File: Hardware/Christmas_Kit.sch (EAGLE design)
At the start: 17 parts, among them U2 ATTINY13DIP, U4 AVR_SPI_PRG_6PTH

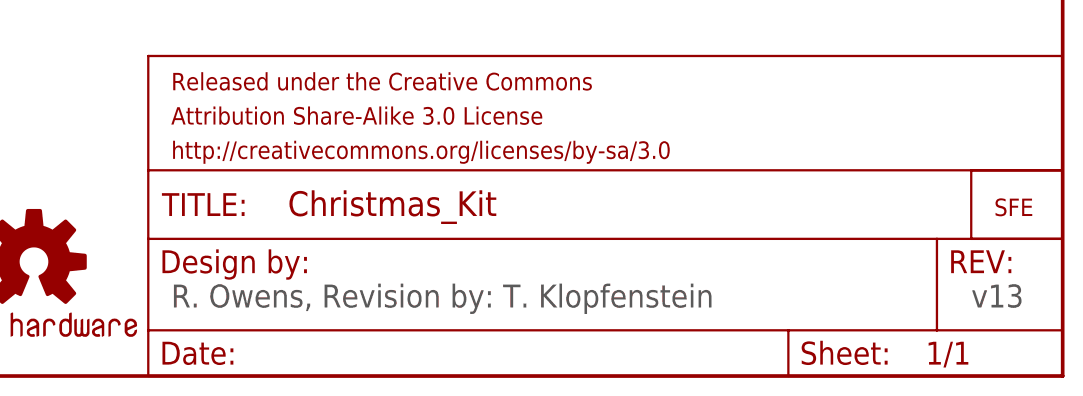
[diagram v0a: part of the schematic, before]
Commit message: Updated revision to symbol
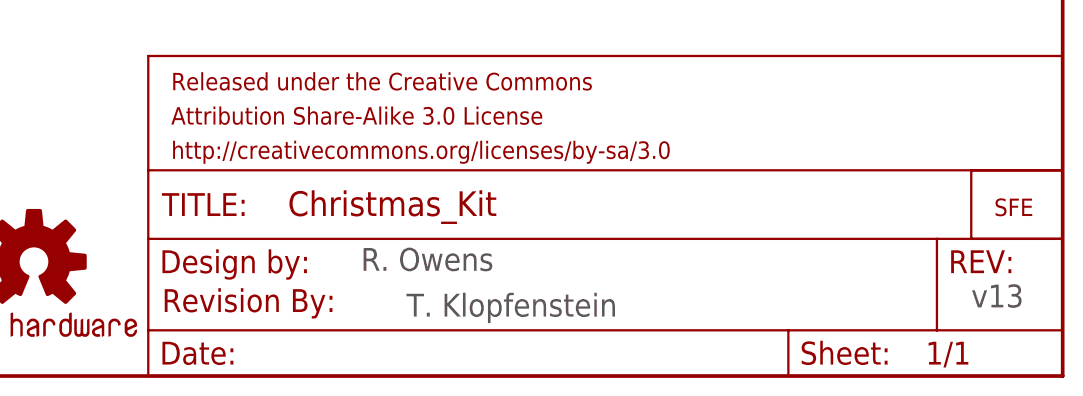
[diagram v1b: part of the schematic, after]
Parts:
- added U$1: REVISION, SparkFun-Aesthetics:REVISION
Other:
- note added: "R. Owens"
- note added: "T. Klopfenstein"
- note removed: "R. Owens, Revision by: T. Klopfenstein"
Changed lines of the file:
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@@
 <grid distance="0.1" unitdist="inch" unit="inch" style="lines" multiple="1" display="no" altdistance="0.01" altunitdist="inch" altunit="inch"/>
 <layers>
-<layer number="1" name="Top" color="4" fill="1" visible="yes" active="no"/>
-<layer number="2" name="Route2" color="1" fill="3" visible="yes" active="no"/>
-<layer number="3" name="Route3" color="4" fill="3" visible="yes" active="no"/>
-<layer number="4" name="Route4" color="1" fill="4" visible="yes" active="no"/>
-<layer number="5" name="Route5" color="4" fill="4" visible="yes" active="no"/>
-<layer number="6" name="Route6" color="1" fill="8" visible="yes" active="no"/>
-<layer number="7" name="Route7" color="4" fill="8" visible="yes" active="no"/>
-<layer number="8" name="Route8" color="1" fill="2" visible="yes" active="no"/>
-<layer number="9" name="Route9" color="4" fill="2" visible="yes" active="no"/>
-<layer number="10" name="Route10" color="1" fill="7" visible="yes" active="no"/>
-<layer number="11" name="Route11" color="4" fill="7" visible="yes" active="no"/>
-<layer number="12" name="Route12" color="1" fill="5" visible="yes" active="no"/>
-<layer number="13" name="Route13" color="4" fill="5" visible="yes" active="no"/>
-<layer number="14" name="Route14" color="1" fill="6" visible="yes" active="no"/>
-<layer number="15" name="Route15" color="4" fill="6" visible="yes" active="no"/>
-<layer number="16" name="Bottom" color="1" fill="1" visible="yes" active="no"/>
-<layer number="17" name="Pads" color="2" fill="1" visible="yes" active="no"/>
-<layer number="18" name="Vias" color="2" fill="1" visible="yes" active="no"/>
-<layer number="19" name="Unrouted" color="6" fill="1" visible="yes" active="no"/>
-<layer number="20" name="Dimension" color="15" fill="1" visible="yes" active="no"/>
-<layer number="21" name="tPlace" color="16" fill="1" visible="yes" active="no"/>
-<layer number="22" name="bPlace" color="14" fill="1" visible="yes" active="no"/>
-<layer number="23" name="tOrigins" color="15" fill="1" visible="yes" active="no"/>
-<layer number="24" name="bOrigins" color="15" fill="1" visible="yes" active="no"/>
-<layer number="25" name="tNames" color="7" fill="1" visible="yes" active="no"/>
-<layer number="26" name="bNames" color="7" fill="1" visible="yes" active="no"/>
-<layer number="27" name="tValues" color="7" fill="1" visible="yes" active="no"/>
-<layer number="28" name="bValues" color="7" fill="1" visible="yes" active="no"/>
+<layer number="1" name="Top" color="4" fill="1" visible="no" active="no"/>
+<layer number="2" name="Route2" color="1" fill="3" visible="no" active="no"/>
+<layer number="3" name="Route3" color="4" fill="3" visible="no" active="no"/>
+<layer number="4" name="Route4" color="1" fill="4" visible="no" active="no"/>
+<layer number="5" name="Route5" color="4" fill="4" visible="no" active="no"/>
+<layer number="6" name="Route6" color="1" fill="8" visible="no" active="no"/>
+<layer number="7" name="Route7" color="4" fill="8" visible="no" active="no"/>
+<layer number="8" name="Route8" color="1" fill="2" visible="no" active="no"/>
+<layer number="9" name="Route9" color="4" fill="2" visible="no" active="no"/>
+<layer number="10" name="Route10" color="1" fill="7" visible="no" active="no"/>
+<layer number="11" name="Route11" color="4" fill="7" visible="no" active="no"/>
+<layer number="12" name="Route12" color="1" fill="5" visible="no" active="no"/>
+<layer number="13" name="Route13" color="4" fill="5" visible="no" active="no"/>
+<layer number="14" name="Route14" color="1" fill="6" visible="no" active="no"/>
+<layer number="15" name="Route15" color="4" fill="6" visible="no" active="no"/>
+<layer number="16" name="Bottom" color="1" fill="1" visible="no" active="no"/>
+<layer number="17" name="Pads" color="2" fill="1" visible="no" active="no"/>
+<layer number="18" name="Vias" color="2" fill="1" visible="no" active="no"/>
+<layer number="19" name="Unrouted" color="6" fill="1" visible="no" active="no"/>
+<layer number="20" name="Dimension" color="15" fill="1" visible="no" active="no"/>
+<layer number="21" name="tPlace" color="16" fill="1" visible="no" active="no"/>
+<layer number="22" name="bPlace" color="14" fill="1" visible="no" active="no"/>
+<layer number="23" name="tOrigins" color="15" fill="1" visible="no" active="no"/>
+<layer number="24" name="bOrigins" color="15" fill="1" visible="no" active="no"/>
+<layer number="25" name="tNames" color="7" fill="1" visible="no" active="no"/>
+<layer number="26" name="bNames" color="7" fill="1" visible="no" active="no"/>
+<layer number="27" name="tValues" color="7" fill="1" visible="no" active="no"/>
+<layer number="28" name="bValues" color="7" fill="1" visible="no" active="no"/>
 <layer number="29" name="tStop" color="7" fill="3" visible="no" active="no"/>
 <layer number="30" name="bStop" color="7" fill="6" visible="no" active="no"/>
@@
 <layer number="35" name="tGlue" color="7" fill="4" visible="no" active="no"/>
 <layer number="36" name="bGlue" color="7" fill="5" visible="no" active="no"/>
-<layer number="37" name="tTest" color="7" fill="1" visible="yes" active="no"/>
-<layer number="38" name="bTest" color="7" fill="1" visible="yes" active="no"/>
+<layer number="37" name="tTest" color="7" fill="1" visible="no" active="no"/>
+<layer number="38" name="bTest" color="7" fill="1" visible="no" active="no"/>
 <layer number="39" name="tKeepout" color="4" fill="11" visible="no" active="no"/>
 <layer number="40" name="bKeepout" color="1" fill="11" visible="no" active="no"/>
@@
 <layer number="44" name="Drills" color="7" fill="1" visible="no" active="no"/>
 <layer number="45" name="Holes" color="7" fill="1" visible="no" active="no"/>
-<layer number="46" name="Milling" color="3" fill="1" visible="yes" active="no"/>
-<layer number="47" name="Measures" color="7" fill="1" visible="yes" active="no"/>
-<layer number="48" name="Document" color="7" fill="1" visible="yes" active="no"/>
-<layer number="49" name="Reference" color="7" fill="1" visible="yes" active="no"/>
-<layer number="50" name="dxf" color="7" fill="1" visible="yes" active="no"/>
-<layer number="51" name="tDocu" color="6" fill="1" visible="yes" active="no"/>
-<layer number="52" name="bDocu" color="7" fill="1" visible="yes" active="no"/>
-<layer number="53" name="tGND_GNDA" color="7" fill="9" visible="yes" active="no"/>
-<layer number="54" name="bGND_GNDA" color="1" fill="9" visible="yes" active="no"/>
-<layer number="56" name="wert" color="7" fill="1" visible="yes" active="no"/>
+<layer number="46" name="Milling" color="3" fill="1" visible="no" active="no"/>
+<layer number="47" name="Measures" color="7" fill="1" visible="no" active="no"/>
+<layer number="48" name="Document" color="7" fill="1" visible="no" active="no"/>
+<layer number="49" name="Reference" color="7" fill="1" visible="no" active="no"/>
+<layer number="50" name="dxf" color="7" fill="1" visible="no" active="no"/>
+<layer number="51" name="tDocu" color="6" fill="1" visible="no" active="no"/>
+<layer number="52" name="bDocu" color="7" fill="1" visible="no" active="no"/>
+<layer number="53" name="tGND_GNDA" color="7" fill="9" visible="no" active="no"/>
+<layer number="54" name="bGND_GNDA" color="1" fill="9" visible="no" active="no"/>
+<layer number="56" name="wert" color="7" fill="1" visible="no" active="no"/>
 <layer number="91" name="Nets" color="2" fill="1" visible="yes" active="yes"/>
 <layer number="92" name="Busses" color="1" fill="1" visible="yes" active="yes"/>
@@
 <part name="LED10" library="SparkFun" deviceset="LED" device="5MM" value="GREEN"/>
 <part name="LOGO1" library="SparkFun-Aesthetics" deviceset="OSHW-LOGO" device="L"/>
+<part name="U$1" library="SparkFun-Aesthetics" deviceset="REVISION" device=""/>
 </parts>
 <sheets>
 <sheet>
 <plain>
-<text x="149.86" y="7.62" size="2.54" layer="97">R. Owens, Revision by: T. Klopfenstein</text>
+<text x="170.942" y="11.684" size="2.54" layer="97">R. Owens</text>
 <text x="238.76" y="7.62" size="2.54" layer="97">v13</text>
+<text x="176.022" y="6.604" size="2.54" layer="97">T. Klopfenstein</text>
 </plain>
 <instances>
@@
 </instance>
 <instance part="LOGO1" gate="G$1" x="134.62" y="12.7"/>
+<instance part="U$1" gate="G$1" x="148.844" y="7.112"/>
 </instances>
 <busses>
